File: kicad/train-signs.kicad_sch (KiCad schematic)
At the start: 3 parts, among them J1 Conn_02x10_Odd_Even

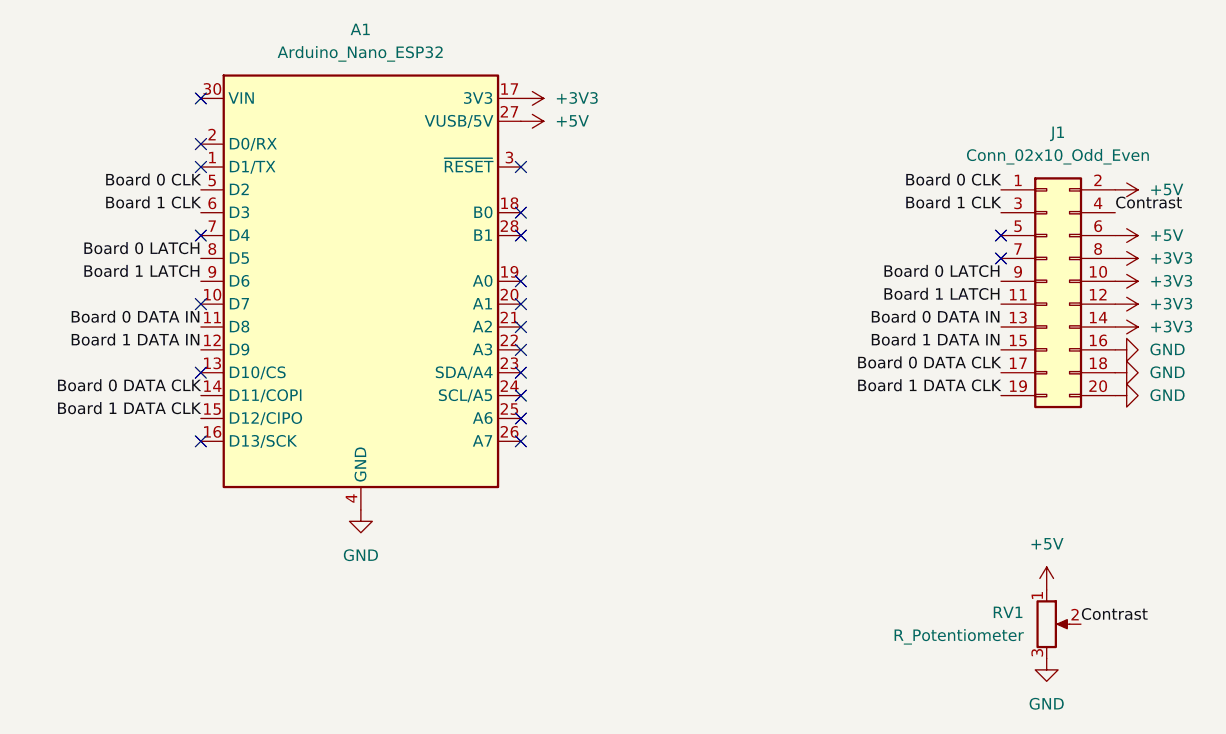
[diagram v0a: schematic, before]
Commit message: Correct KiCAD schema
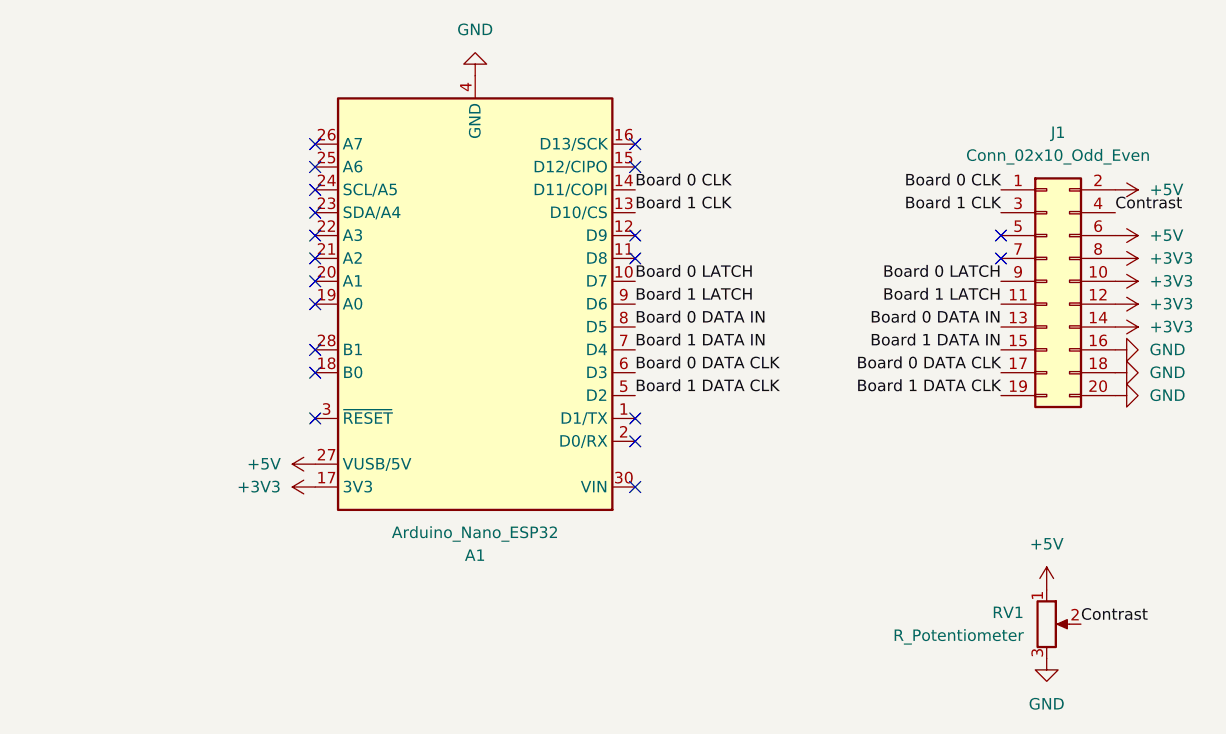
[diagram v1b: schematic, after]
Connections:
- net Board 0 CLK: now also A1.14 (D11/COPI); no longer A1.5 (D2)
- net Board 0 DATA CLK: now also A1.6 (D3); no longer A1.14 (D11/COPI)
- net Board 0 DATA IN: now also A1.8 (D5); no longer A1.11 (D8)
- net Board 0 LATCH: now also A1.10 (D7); no longer A1.8 (D5)
- net Board 1 CLK: now also A1.13 (D10/CS); no longer A1.6 (D3)
- net Board 1 DATA CLK: now also A1.5 (D2); no longer A1.15 (D12/CIPO)
- net Board 1 DATA IN: now also A1.7 (D4); no longer A1.12 (D9)
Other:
- moved on the sheet: A1
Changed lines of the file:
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@@
 	(paper "A4")
 	(no_connect
-		(at 45.72 78.74)
-	)
-	(no_connect
-		(at 81.28 76.2)
-	)
-	(no_connect
-		(at 81.28 93.98)
-	)
-	(no_connect
-		(at 81.28 83.82)
-	)
-	(no_connect
-		(at 81.28 86.36)
-	)
-	(no_connect
-		(at 81.28 71.12)
-	)
-	(no_connect
-		(at 45.72 63.5)
-	)
-	(no_connect
-		(at 45.72 86.36)
+		(at 58.42 78.74)
+	)
+	(no_connect
+		(at 58.42 60.96)
+	)
+	(no_connect
+		(at 58.42 71.12)
+	)
+	(no_connect
+		(at 58.42 68.58)
+	)
+	(no_connect
+		(at 93.98 99.06)
+	)
+	(no_connect
+		(at 58.42 83.82)
+	)
+	(no_connect
+		(at 93.98 63.5)
+	)
+	(no_connect
+		(at 93.98 91.44)
 	)
 	(no_connect
@@
 	)
 	(no_connect
-		(at 81.28 78.74)
-	)
-	(no_connect
-		(at 81.28 68.58)
-	)
-	(no_connect
-		(at 81.28 91.44)
+		(at 58.42 76.2)
+	)
+	(no_connect
+		(at 58.42 86.36)
+	)
+	(no_connect
+		(at 58.42 63.5)
 	)
 	(no_connect
@@
 	)
 	(no_connect
-		(at 81.28 88.9)
-	)
-	(no_connect
-		(at 45.72 93.98)
-	)
-	(no_connect
-		(at 45.72 71.12)
-	)
-	(no_connect
-		(at 81.28 81.28)
-	)
-	(no_connect
-		(at 81.28 63.5)
-	)
-	(no_connect
-		(at 45.72 55.88)
-	)
-	(no_connect
-		(at 45.72 60.96)
-	)
-	(label "Board 1 LATCH"
-		(at 45.72 76.2 180)
-		(effects
-			(font
-				(size 1.27 1.27)
-			)
-			(justify right bottom)
+		(at 93.98 71.12)
+	)
+	(no_connect
+		(at 93.98 73.66)
+	)
+	(no_connect
+		(at 58.42 66.04)
+	)
+	(no_connect
+		(at 93.98 93.98)
+	)
+	(no_connect
+		(at 58.42 73.66)
+	)
+	(no_connect
+		(at 58.42 91.44)
+	)
+	(no_connect
+		(at 93.98 60.96)
+	)
+	(label "Board 0 DATA CLK"
+		(at 93.98 86.36 0)
+		(effects
+			(font
+				(size 1.27 1.27)
+			)
+			(justify left bottom)
 		)
 	)
@@
 		)
 	)
+	(label "Board 1 DATA CLK"
+		(at 93.98 88.9 0)
+		(effects
+			(font
+				(size 1.27 1.27)
+			)
+			(justify left bottom)
+		)
+	)
 	(label "Board 0 CLK"
 		(at 134.62 66.04 180)
@@
 	)
 	(label "Board 0 CLK"
-		(at 45.72 66.04 180)
-		(effects
-			(font
-				(size 1.27 1.27)
-			)
-			(justify right bottom)
+		(at 93.98 66.04 0)
+		(effects
+			(font
+				(size 1.27 1.27)
+			)
+			(justify left bottom)
 		)
 	)
@@
 	)
 	(label "Board 0 DATA IN"
-		(at 45.72 81.28 180)
-		(effects
-			(font
-				(size 1.27 1.27)
-			)
-			(justify right bottom)
+		(at 93.98 81.28 0)
+		(effects
+			(font
+				(size 1.27 1.27)
+			)
+			(justify left bottom)
+		)
+	)
+	(label "Board 1 LATCH"
+		(at 93.98 78.74 0)
+		(effects
+			(font
+				(size 1.27 1.27)
+			)
+			(justify left bottom)
 		)
 	)
 	(label "Board 1 DATA IN"
-		(at 45.72 83.82 180)
-		(effects
-			(font
-				(size 1.27 1.27)
-			)
-			(justify right bottom)
-		)
-	)
-	(label "Board 0 DATA CLK"
-		(at 45.72 88.9 180)
-		(effects
-			(font
-				(size 1.27 1.27)
-			)
-			(justify right bottom)
-		)
-	)
-	(label "Board 1 DATA CLK"
-		(at 45.72 91.44 180)
-		(effects
-			(font
-				(size 1.27 1.27)
-			)
-			(justify right bottom)
+		(at 93.98 83.82 0)
+		(effects
+			(font
+				(size 1.27 1.27)
+			)
+			(justify left bottom)
 		)
 	)
 	(label "Board 1 CLK"
-		(at 45.72 68.58 180)
-		(effects
-			(font
-				(size 1.27 1.27)
-			)
-			(justify right bottom)
+		(at 93.98 68.58 0)
+		(effects
+			(font
+				(size 1.27 1.27)
+			)
+			(justify left bottom)
+		)
+	)
+	(label "Board 0 LATCH"
+		(at 93.98 76.2 0)
+		(effects
+			(font
+				(size 1.27 1.27)
+			)
+			(justify left bottom)
 		)
 	)
@@
 		)
 	)
-	(label "Board 0 LATCH"
-		(at 45.72 73.66 180)
-		(effects
-			(font
-				(size 1.27 1.27)
-			)
-			(justify right bottom)
-		)
-	)
 	(symbol
 		(lib_id "Device:R_Potentiometer")
@@
 	(symbol
 		(lib_id "power:+5V")
-		(at 81.28 58.42 270)
+		(at 58.42 96.52 90)
 		(unit 1)
 		(exclude_from_sim no)
@@
 		(fields_autoplaced yes)
 		(property "Reference" "#PWR01"
-			(at 77.47 58.42 0)
+			(at 62.23 96.52 0)
 			(effects
 				(font
@@
 		)
 		(property "Value" "+5V"
-			(at 85.09 58.4199 90)
+			(at 54.61 96.5201 90)
 			(effects
 				(font
@@
 		)
 		(property "Footprint" ""
-			(at 81.28 58.42 0)
+			(at 58.42 96.52 0)
 			(effects
 				(font
@@
 		)
 		(property "Datasheet" ""
-			(at 81.28 58.42 0)
+			(at 58.42 96.52 0)
 			(effects
 				(font
@@
 		)
 		(property "Description" "Power symbol creates a global label with name \"+5V\""
-			(at 81.28 58.42 0)
+			(at 58.42 96.52 0)
 			(effects
 				(font
@@
 	(symbol
 		(lib_id "power:GND")
-		(at 63.5 101.6 0)
+		(at 76.2 53.34 180)
 		(unit 1)
 		(exclude_from_sim no)
@@
 		(fields_autoplaced yes)
 		(property "Reference" "#PWR03"
-			(at 63.5 107.95 0)
+			(at 76.2 46.99 0)
 			(effects
 				(font
@@
 		)
 		(property "Value" "GND"
-			(at 63.5 106.68 0)
-			(effects
-				(font
-					(size 1.27 1.27)
-				)
-			)
-		)
-		(property "Footprint" ""
-			(at 63.5 101.6 0)
+			(at 76.2 48.26 0)
+			(effects
+				(font
+					(size 1.27 1.27)
+				)
+			)
+		)
+		(property "Footprint" ""
+			(at 76.2 53.34 0)
 			(effects
 				(font
@@
 		)
 		(property "Datasheet" ""
-			(at 63.5 101.6 0)
+			(at 76.2 53.34 0)
 			(effects
 				(font
@@
 		)
 		(property "Description" "Power symbol creates a global label with name \"GND\" , ground"
-			(at 63.5 101.6 0)
+			(at 76.2 53.34 0)
 			(effects
 				(font
@@
 	(symbol
 		(lib_id "power:+3V3")
-		(at 81.28 55.88 270)
+		(at 58.42 99.06 90)
 		(unit 1)
 		(exclude_from_sim no)
@@
 		(fields_autoplaced yes)
 		(property "Reference" "#PWR02"
-			(at 77.47 55.88 0)
+			(at 62.23 99.06 0)
 			(effects
 				(font
@@
 		)
 		(property "Value" "+3V3"
-			(at 85.09 55.8799 90)
+			(at 54.61 99.0601 90)
 			(effects
 				(font
@@
 		)
 		(property "Footprint" ""
-			(at 81.28 55.88 0)
+			(at 58.42 99.06 0)
 			(effects
 				(font
@@
 		)
 		(property "Datasheet" ""
-			(at 81.28 55.88 0)
+			(at 58.42 99.06 0)
 			(effects
 				(font
@@
 		)
 		(property "Description" "Power symbol creates a global label with name \"+3V3\""
-			(at 81.28 55.88 0)
+			(at 58.42 99.06 0)
 			(effects
 				(font
@@
 	(symbol
 		(lib_id "MCU_Module:Arduino_Nano_ESP32")
-		(at 63.5 76.2 0)
-		(unit 1)
-		(exclude_from_sim no)
-		(in_bom yes)
-		(on_board yes)
-		(dnp no)
-		(fields_autoplaced yes)
+		(at 76.2 78.74 180)
+		(unit 1)
+		(exclude_from_sim no)
+		(in_bom yes)
+		(on_board yes)
+		(dnp no)
 		(property "Reference" "A1"
-			(at 63.5 48.26 0)
+			(at 76.2 106.68 0)
 			(effects
 				(font
@@
 		)
 		(property "Value" "Arduino_Nano_ESP32"
-			(at 63.5 50.8 0)
+			(at 76.2 104.14 0)
 			(effects
 				(font
@@
 		)
 		(property "Footprint" "Module:Arduino_Nano"
-			(at 77.216 110.236 0)
+			(at 62.484 44.704 0)
 			(effects
 				(font
@@
 		)
 		(property "Datasheet" "https://docs.arduino.cc/resources/datasheets/ABX00083-datasheet.pdf"
-			(at 102.616 107.696 0)
+			(at 37.084 47.244 0)
 			(effects
 				(font
@@
 		)
 		(property "Description" "Arduino Nano board based on the ESP32-S3 with a dual-core 240 MHz processor, 384 kB ROM, 512 kB SRAM. Operates at 3.3V, with 5V USB-C® input and 6-21V VIN. Features Wi-Fi®, Bluetooth® LE, digital and analog pins, and supports SPI, I2C, UART, I2S, and CAN."
-			(at 201.93 105.156 0)
-			(effects
-				(font
+			(at -62.23 49.784 0)
+			(effects
+				(font

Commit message: Update the schematic with XIAO Seeed ESP32C3 and build a PCB
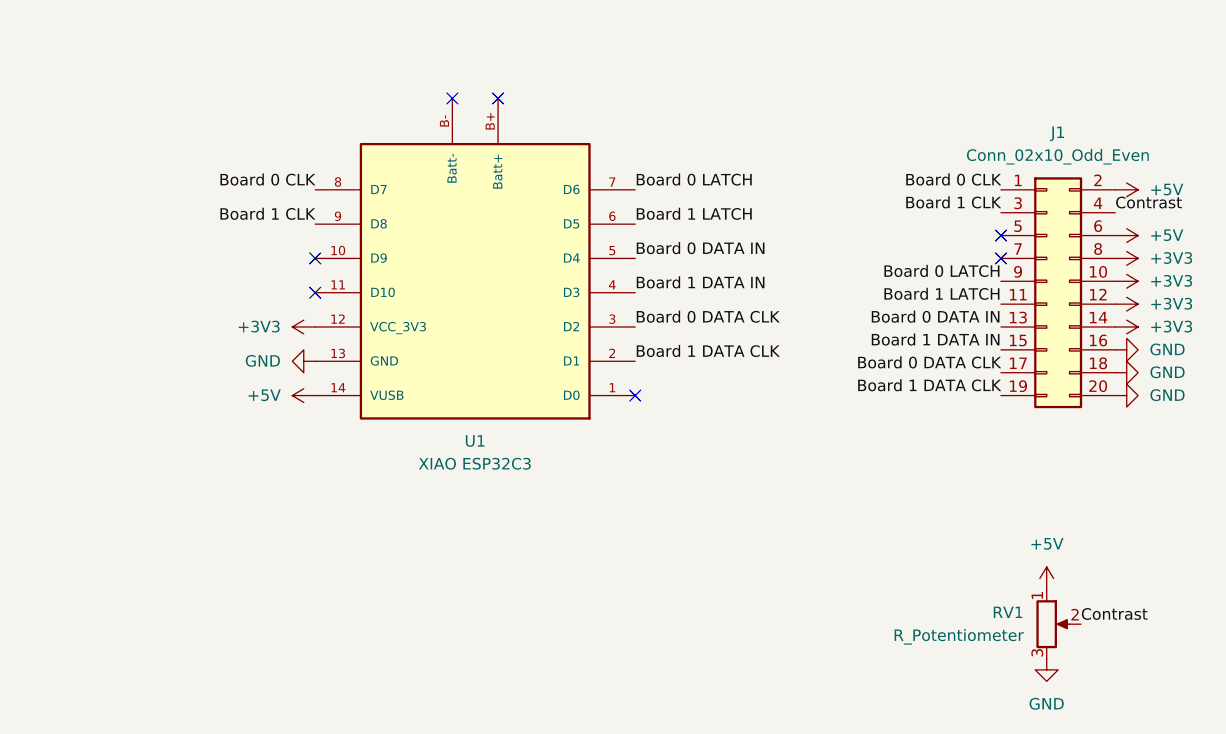
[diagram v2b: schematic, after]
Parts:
- removed A1: Arduino_Nano_ESP32, Module:Arduino_Nano, symbol MCU_Module:Arduino_Nano_ESP32
- added U1: XIAO ESP32C3, kicad-footprints:XIAO Seeed ESP32C3 DIP, symbol kicad-symbols:XIAO ESP32C3
- J1: footprint (none) -> Connector_IDC:IDC-Header_2x10_P2.54mm_Vertical
- RV1: footprint (none) -> kicad-footprints:Potentiometer_Taiwan_Alpha_9mm_Vertical
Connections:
- net +3V3: now also U1.12 (VCC_3V3)
- net +5V: now also U1.14 (VUSB)
- net Board 0 CLK: now also U1.8 (D7)
- net Board 0 DATA CLK: now also U1.3 (D2)
- net Board 0 DATA IN: now also U1.5 (D4)
- net Board 0 LATCH: now also U1.7 (D6)
- net Board 1 CLK: now also U1.9 (D8)
- net Board 1 DATA CLK: now also U1.2 (D1)
- net Board 1 DATA IN: now also U1.4 (D3)
- net Board 1 LATCH: now also U1.6 (D5)
- net GND: now also U1.13 (GND)
- no-connect marks 20 -> 7
